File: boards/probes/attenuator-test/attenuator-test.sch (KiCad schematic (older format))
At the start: 8 parts, among them J1 Conn_Coaxial, J2 Conn_Coaxial

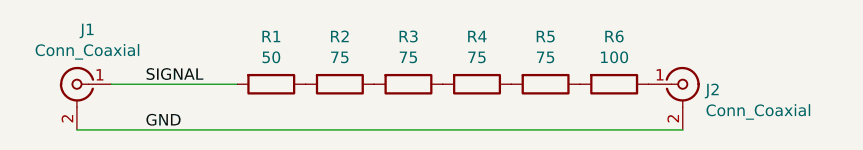
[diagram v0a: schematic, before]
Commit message: Updated attenuator test with 4 overlapping resistor footprints
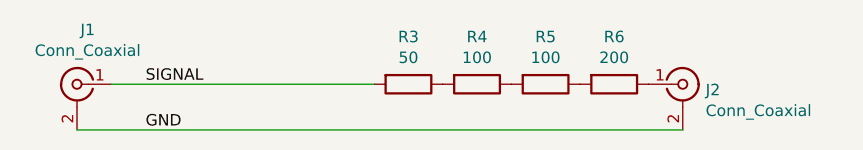
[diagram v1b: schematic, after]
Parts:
- removed R1: 50, azonenberg_pcb:EIA_0402_RES_NOSILK_FLIPCHIP, symbol device:R
- removed R2: 75, azonenberg_pcb:EIA_0402_RES_NOSILK_FLIPCHIP, symbol device:R
- R3: value 75 -> 50
- R4, R5: value 75 -> 100
- R6: value 100 -> 200
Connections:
- net SIGNAL: now also R3.2
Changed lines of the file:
@@
 EESchema Schematic File Version 4
+LIBS:attenuator-test-cache
 EELAYER 30 0
 EELAYER END
@@
 Sheet 1 1
 Title ""
-Date ""
+Date "2020-08-30"
 Rev ""
 Comp ""
@@
 SIGNAL
 $Comp
-L device:R R1
-U 1 1 5F20581A
-P 4600 2500
-F 0 "R1" V 4393 2500 50  0000 C CNN
-F 1 "50" V 4484 2500 50  0000 C CNN
-F 2 "azonenberg_pcb:EIA_0402_RES_NOSILK_FLIPCHIP" V 4530 2500 50  0001 C CNN
-F 3 "" H 4600 2500 50  0001 C CNN
-	1    4600 2500
-	0    1    1    0
-$EndComp
-Wire Wire Line
-	3900 2500 4450 2500
-$Comp
-L device:R R2
-U 1 1 5F205C5D
-P 4900 2500
-F 0 "R2" V 4693 2500 50  0000 C CNN
-F 1 "75" V 4784 2500 50  0000 C CNN
-F 2 "azonenberg_pcb:EIA_0402_RES_NOSILK_FLIPCHIP" V 4830 2500 50  0001 C CNN
-F 3 "" H 4900 2500 50  0001 C CNN
-	1    4900 2500
-	0    1    1    0
-$EndComp
-$Comp
 L device:R R3
 U 1 1 5F205EF6
 P 5200 2500
 F 0 "R3" V 4993 2500 50  0000 C CNN
-F 1 "75" V 5084 2500 50  0000 C CNN
+F 1 "50" V 5084 2500 50  0000 C CNN
 F 2 "azonenberg_pcb:EIA_0402_RES_NOSILK_FLIPCHIP" V 5130 2500 50  0001 C CNN
 F 3 "" H 5200 2500 50  0001 C CNN
@@
 P 5500 2500
 F 0 "R4" V 5293 2500 50  0000 C CNN
-F 1 "75" V 5384 2500 50  0000 C CNN
+F 1 "100" V 5384 2500 50  0000 C CNN
 F 2 "azonenberg_pcb:EIA_0402_RES_NOSILK_FLIPCHIP" V 5430 2500 50  0001 C CNN
 F 3 "" H 5500 2500 50  0001 C CNN
@@
 P 5800 2500
 F 0 "R5" V 5593 2500 50  0000 C CNN
-F 1 "75" V 5684 2500 50  0000 C CNN
+F 1 "100" V 5684 2500 50  0000 C CNN
 F 2 "azonenberg_pcb:EIA_0402_RES_NOSILK_FLIPCHIP" V 5730 2500 50  0001 C CNN
 F 3 "" H 5800 2500 50  0001 C CNN
@@
 P 6100 2500
 F 0 "R6" V 5893 2500 50  0000 C CNN
-F 1 "100" V 5984 2500 50  0000 C CNN
+F 1 "200" V 5984 2500 50  0000 C CNN
 F 2 "azonenberg_pcb:EIA_0402_RES_NOSILK_FLIPCHIP" V 6030 2500 50  0001 C CNN
 F 3 "" H 6100 2500 50  0001 C CNN
@@
 Wire Wire Line
 	6400 2700 3750 2700
+Wire Wire Line
+	3900 2500 5050 2500
 $EndSCHEMATC

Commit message: Attenuator test with 3 resistors
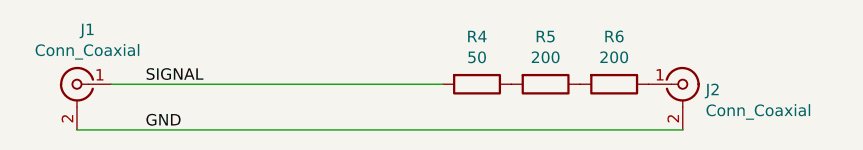
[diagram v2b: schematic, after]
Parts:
- removed R3: 50, azonenberg_pcb:EIA_0402_RES_NOSILK_FLIPCHIP, symbol device:R
- R4: value 100 -> 50
- R5: value 100 -> 200
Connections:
- net SIGNAL: now also R4.2
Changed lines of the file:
@@
 SIGNAL
-$Comp
-L device:R R3
-U 1 1 5F205EF6
-P 5200 2500
-F 0 "R3" V 4993 2500 50  0000 C CNN
-F 1 "50" V 5084 2500 50  0000 C CNN
-F 2 "azonenberg_pcb:EIA_0402_RES_NOSILK_FLIPCHIP" V 5130 2500 50  0001 C CNN
-F 3 "" H 5200 2500 50  0001 C CNN
-	1    5200 2500
-	0    1    1    0
-$EndComp
 $Comp
 L device:R R4
@@
 P 5500 2500
 F 0 "R4" V 5293 2500 50  0000 C CNN
-F 1 "100" V 5384 2500 50  0000 C CNN
+F 1 "50" V 5384 2500 50  0000 C CNN
 F 2 "azonenberg_pcb:EIA_0402_RES_NOSILK_FLIPCHIP" V 5430 2500 50  0001 C CNN
 F 3 "" H 5500 2500 50  0001 C CNN
@@
 P 5800 2500
 F 0 "R5" V 5593 2500 50  0000 C CNN
-F 1 "100" V 5684 2500 50  0000 C CNN
+F 1 "200" V 5684 2500 50  0000 C CNN
 F 2 "azonenberg_pcb:EIA_0402_RES_NOSILK_FLIPCHIP" V 5730 2500 50  0001 C CNN
 F 3 "" H 5800 2500 50  0001 C CNN
@@
 	6400 2700 3750 2700
 Wire Wire Line
-	3900 2500 5050 2500
+	3900 2500 5350 2500
 $EndSCHEMATC
